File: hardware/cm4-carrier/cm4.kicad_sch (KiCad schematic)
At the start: 2 parts, among them J3 Raspberry Pi CM4

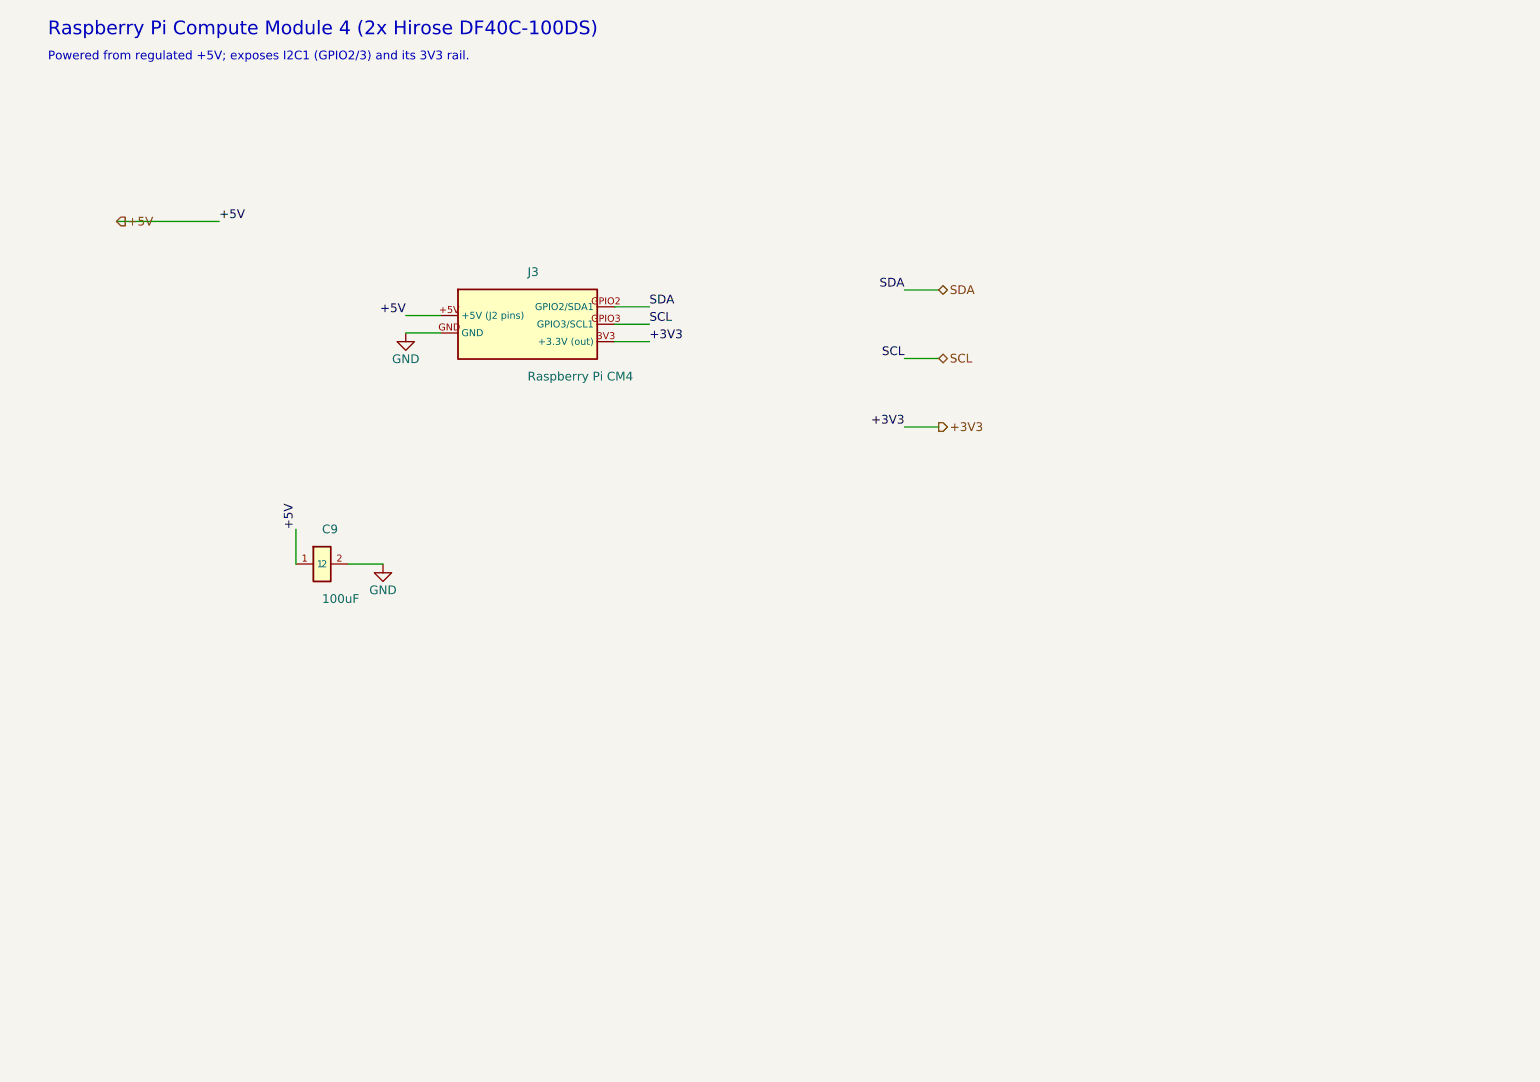
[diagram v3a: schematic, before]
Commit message: Add proper Raspberry Pi CM4 symbol and footprint
Replace the 5-pin CM4 placeholder with a real representation: the module is
modeled as its two physical 100-pin Hirose DF40 connectors (J3 = connector 1,
J4 = connector 2), each mapped to the carrier-side mating footprint
Connector_Hirose_DF40:Hirose_DF40C-100DP-0.4V_2x50-1MP_P0.4mm, with the full,
correctly-numbered CM4 pinout on every pin.

The board wires what it uses: all six +5V input pins, every GND on both
connectors, GPIO2/GPIO3 (I2C1) to the fuel gauge, and GPIO_VREF +
CM4_3.3V_Out for the 3.3 V I/O rail (which also feeds the I2C pull-ups). The
high-speed interfaces (PCIe, USB, Ethernet, HDMI, CSI/DSI) are left available
on the connectors. Adds C12 for CM4 5 V decoupling.

Pin maps were taken from the Kedarius RPi-CM4-Kicad symbol and cross-checked
against known CM4 facts (5 V on J1 77/79/81/83/85/87; GPIO2=pin58=SDA1;
GPIO3=pin56=SCL1; CM4_3.3V_Out on J1 84/86). Footprint verified against the
KiCad Connector_Hirose_DF40 library. README/BOM updated with CM4 bring-up
notes. No schematic-format change (KiCad 10, 20260306).

Co-Authored-By: Claude Opus 4.8 <noreply@anthropic.com>
Claude-Session: https://claude.ai/code/session_015B7X7FE461jFSRaiTFdnFt
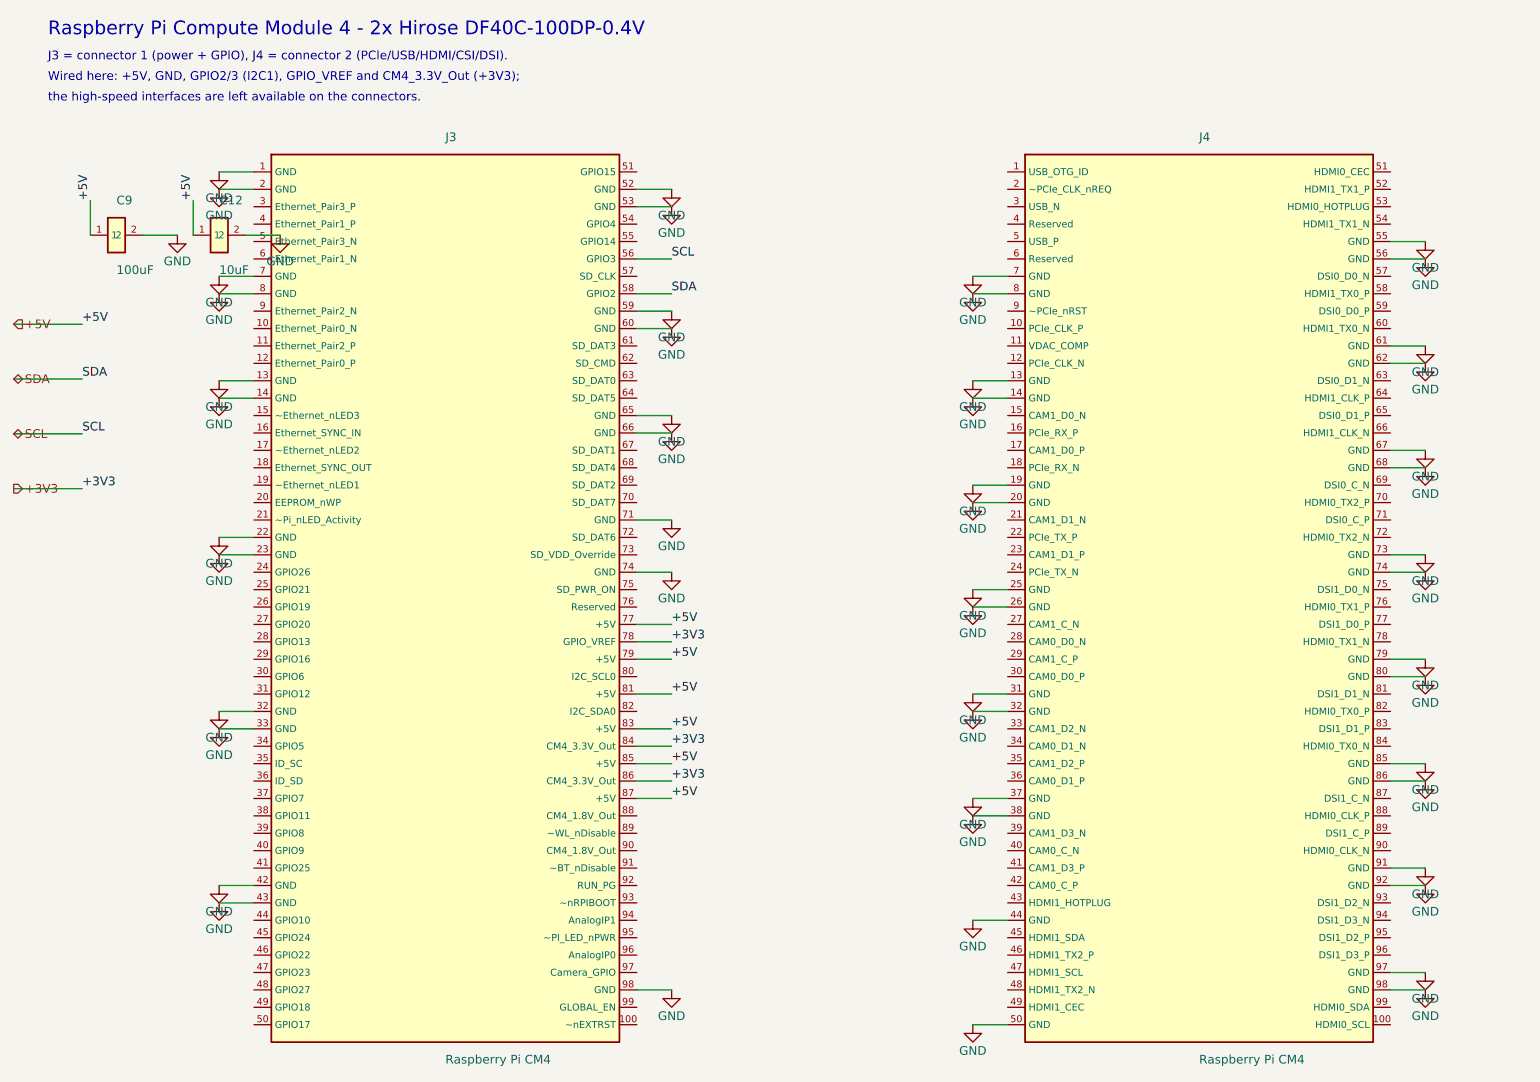
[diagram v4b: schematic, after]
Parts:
- removed J3: Raspberry Pi CM4, Connector_Hirose:Raspberry_Pi_CM4_DF40C-100DS, symbol carrier:Raspberry_Pi_CM4
- added C12: 10uF, Capacitor_SMD:C_0805_2012Metric, symbol carrier:C
- added J3: Raspberry Pi CM4, Connector_Hirose_DF40:Hirose_DF40C-100DP-0.4V_2x50-1MP_P0.4mm, symbol carrier:Raspberry_Pi_CM4_J1
- added J4: Raspberry Pi CM4, Connector_Hirose_DF40:Hirose_DF40C-100DP-0.4V_2x50-1MP_P0.4mm, symbol carrier:Raspberry_Pi_CM4_J2
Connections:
- net +3V3: now also J3.78 (GPIO_VREF), J3.84 (CM4_3.3V_Out), J3.86 (CM4_3.3V_Out)
- net +5V: now also C12.1, J3.77 (+5V), J3.79 (+5V), J3.81 (+5V), J3.83 (+5V), J3.85 (+5V), J3.87 (+5V)
- net GND: now also C12.2, J3.1 (GND), J3.13 (GND), J3.14 (GND), J3.2 (GND), J3.22 (GND), J3.23 (GND), J3.32 (GND), J3.33 (GND), J3.42 (GND), J3.43 (GND), J3.52 (GND), J3.53 (GND), J3.59 (GND), J3.60 (GND), J3.65 (GND), J3.66 (GND), J3.7 (GND), J3.71 (GND), J3.74 (GND), J3.8 (GND), J3.98 (GND), J4.13 (GND), J4.14 (GND), J4.19 (GND), J4.20 (GND), J4.25 (GND), J4.26 (GND), J4.31 (GND), J4.32 (GND), J4.37 (GND), J4.38 (GND), J4.44 (GND), J4.50 (GND), J4.55 (GND), J4.56 (GND), J4.61 (GND), J4.62 (GND), J4.67 (GND), J4.68 (GND), J4.7 (GND), J4.73 (GND), J4.74 (GND), J4.79 (GND), J4.8 (GND), J4.80 (GND), J4.85 (GND), J4.86 (GND), J4.91 (GND), J4.92 (GND), J4.97 (GND), J4.98 (GND)
- net SCL: now also J3.56 (GPIO3)
- net SDA: now also J3.58 (GPIO2)
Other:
- note added: "J3 = connector 1 (power + GPIO), J4 = connector 2 (PCIe/USB/HDMI/CSI/DSI)."
- note added: "Raspberry Pi Compute Module 4 - 2x Hirose DF40C-100DP-0.4V"
- note added: "Wired here: +5V, GND, GPIO2/3 (I2C1), GPIO_VREF and CM4_3.3V_Out (+3V3);"
- note added: "the high-speed interfaces are left available on the connectors."
- note removed: "Powered from regulated +5V; exposes I2C1 (GPIO2/3) and its 3V3 rail."
- note removed: "Raspberry Pi Compute Module 4 (2x Hirose DF40C-100DS)"

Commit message: Add two CSI-2 cameras with I2C mux and camera 3.3V rail
Add a new cameras.kicad_sch sub-sheet providing two Raspberry Pi CSI-2 camera
interfaces:

- J5 (CSI Camera 0) on the CM4's CAM0 (2-lane) interface; J6 (CSI Camera 1)
  on CAM1 (4-lane, two lanes wired) — standard 15-pin 1.0mm Pi camera FFC
  connectors (Connector_FFC-FPC:JUSHUO_AFA07-S15FCA-00...).
- PCA9544A I2C mux (U5) on the camera control bus I2C0 so the two identical-
  address sensors each sit on their own downstream channel (cam0 = ch0,
  cam1 = ch1, mux at 0x70).
- AP2112K-3.3 LDO (U7) generating a dedicated camera 3.3V rail from +5V, so
  two cameras don't overload the CM4's limited CM4_3.3V_Out. Adds per-channel
  and upstream I2C pull-ups and decoupling (R15-R20, C13-C15).

The CM4 sheet now exports the CAM0/CAM1 MIPI lanes (from J4), I2C0
(I2C_SCL0/SDA0) and four spare GPIOs (GPIO4-7, for the camera IO0/IO1
LED/enable lines) as global nets; the cameras sheet consumes them. Camera
FFC pinout and PCA9544A/DF40/FFC footprints were taken from KiCad's
libraries and the standard 15-pin CSI pinout.

Root gains a (pinless) Cameras sheet box. README/BOM updated. No
schematic-format change (KiCad 10, 20260306).

Co-Authored-By: Claude Opus 4.8 <noreply@anthropic.com>
Claude-Session: https://claude.ai/code/session_015B7X7FE461jFSRaiTFdnFt
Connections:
- net CAM1_D0_N: now reaches J4.15 (CAM1_D0_N)
- net CAM1_D0_P: now reaches J4.17 (CAM1_D0_P)
- net CAM1_D1_N: now reaches J4.21 (CAM1_D1_N)
- net CAM1_D1_P: now reaches J4.23 (CAM1_D1_P)
- net CAM1_C_N: now reaches J4.27 (CAM1_C_N)
- net CAM0_D0_N: now reaches J4.28 (CAM0_D0_N)
- net CAM1_C_P: now reaches J4.29 (CAM1_C_P)
- net CAM0_D0_P: now reaches J4.30 (CAM0_D0_P)
- net CAM0_D1_N: now reaches J4.34 (CAM0_D1_N)
- net CAM0_D1_P: now reaches J4.36 (CAM0_D1_P)
- net CAM0_C_N: now reaches J4.40 (CAM0_C_N)
- net CAM0_C_P: now reaches J4.42 (CAM0_C_P)
- net CAM1_IO0: now reaches J3.30 (GPIO6)
- net CAM0_IO1: now reaches J3.34 (GPIO5)
- net CAM1_IO1: now reaches J3.37 (GPIO7)
- net CAM0_IO0: now reaches J3.54 (GPIO4)
- net I2C0_SCL: now reaches J3.80 (I2C_SCL0)
- net I2C0_SDA: now reaches J3.82 (I2C_SDA0)

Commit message: Add a DSI display on the CM4's DSI0 interface
Add a Raspberry Pi DSI display connector (J7) to the peripherals sheet
(now "Cameras & Display"):

- J7 is a standard 15-pin 1.0mm RPi FFC driven by the CM4's DSI0 (2-lane)
  interface; the six DSI0 differential lanes are exported from the CM4 sheet
  (J4) as global nets alongside the camera lanes.
- The display's touch/controller I2C shares I2C0 on PCA9544A mux channel 2
  (SD2/SC2, previously unused), with its own pull-ups (R21/R22).
- IO0/IO1 (reset / backlight-enable) route to CM4 GPIO8/GPIO9; 3.3V logic
  comes from the existing camera LDO rail. The 5V panel/backlight power is
  supplied separately, as on the standard RPi 7-inch panel.

The mux is now 3 of 4 channels used (cam0/cam1/display). Root box renamed to
"Cameras & Display". README/BOM updated. No format change (KiCad 10, 20260306).

Co-Authored-By: Claude Opus 4.8 <noreply@anthropic.com>
Claude-Session: https://claude.ai/code/session_015B7X7FE461jFSRaiTFdnFt
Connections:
- net DSI0_D0_N: now reaches J4.57 (DSI0_D0_N)
- net DSI0_D0_P: now reaches J4.59 (DSI0_D0_P)
- net DSI0_D1_N: now reaches J4.63 (DSI0_D1_N)
- net DSI0_D1_P: now reaches J4.65 (DSI0_D1_P)
- net DSI0_C_N: now reaches J4.69 (DSI0_C_N)
- net DSI0_C_P: now reaches J4.71 (DSI0_C_P)
- net DSI0_IO0: now reaches J3.39 (GPIO8)
- net DSI0_IO1: now reaches J3.40 (GPIO9)

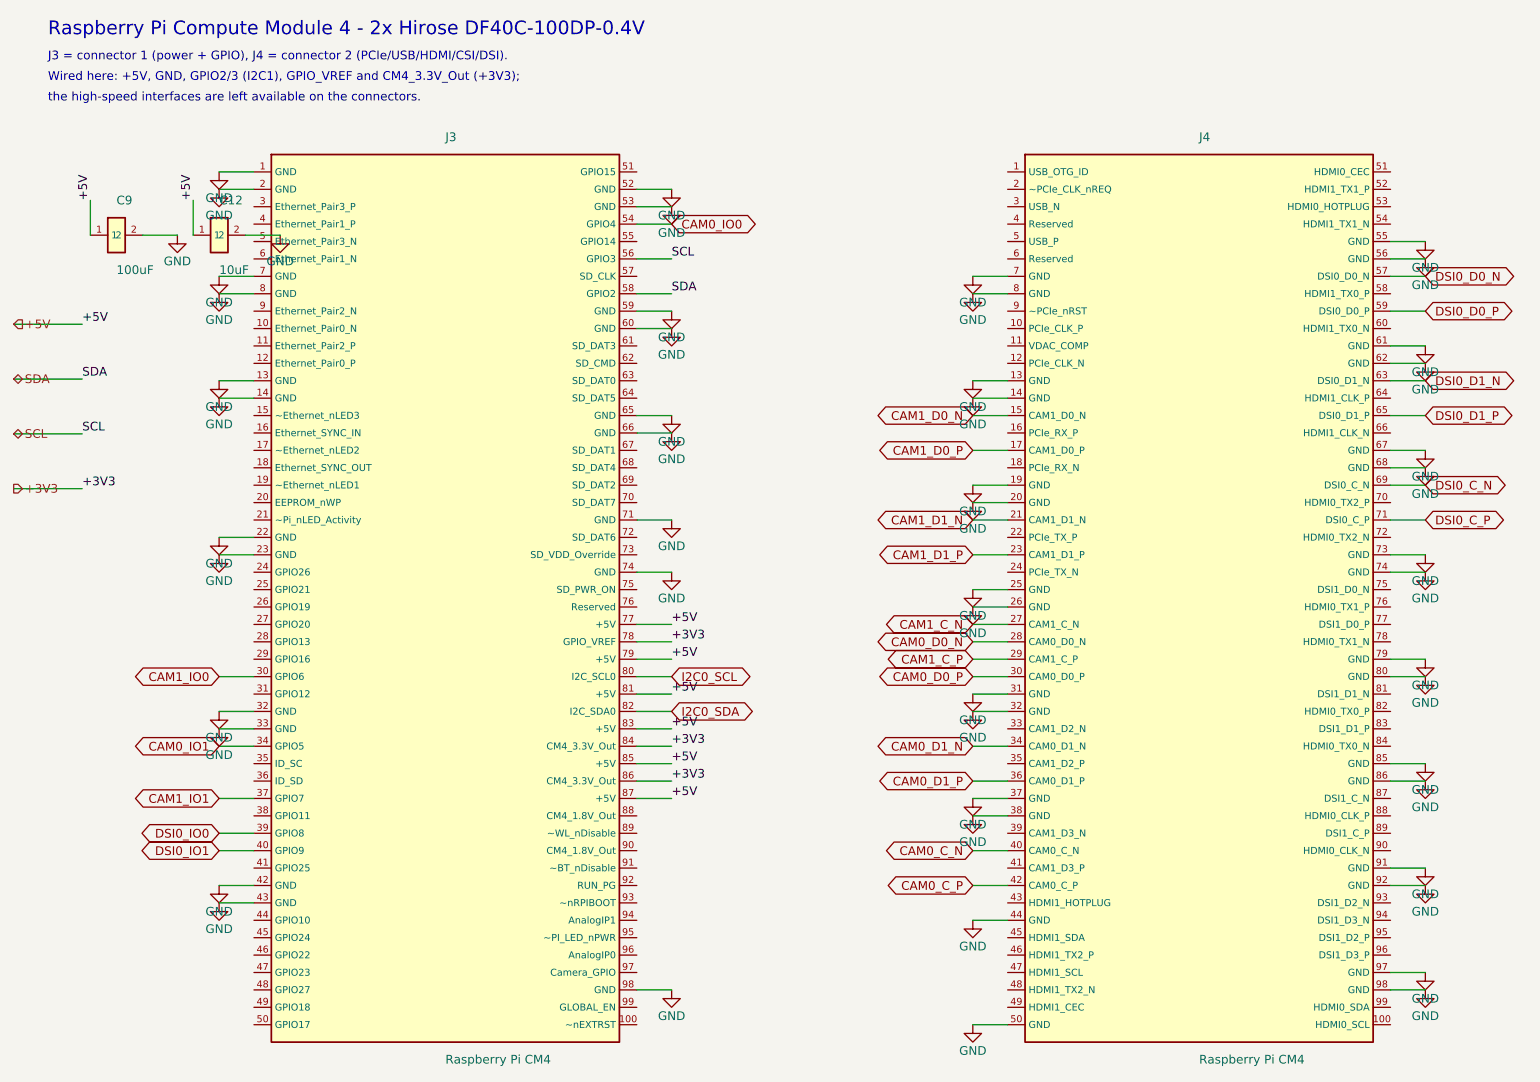
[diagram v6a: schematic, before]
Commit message: Add microSD boot (CM4 Lite) and CM4 bring-up controls
Add a boot_sd.kicad_sch sub-sheet with a microSD socket and the CM4 module
bring-up controls, so a CM4 Lite (no eMMC) can boot from card:

- microSD socket (J8, Hirose DM3D-SF) wired to the CM4 SD interface
  (SD_CLK/SD_CMD/SD_DAT0-3) with CMD/DAT pull-ups and a card-detect pull-up.
- SD 3.3V is gated by a high-side load switch (Q2 P-FET + Q3 N-FET) driven by
  the CM4's SD_PWR_ON (active high), with the card rail decoupled (C16/C17).
  SD_VDD_Override is defaulted low (3.3V card).
- Bring-up controls: GLOBAL_EN (power/enable, SW1), RUN_PG (run/reset, SW2)
  and nRPIBOOT (USB/rpiboot, SW3), each with a pull-up and momentary button;
  nEXTRST pulled up; power/activity LEDs (D3/D4) on PI_LED_nPWR / PI_LED_ACT.

The CM4 sheet now exports the SD interface and the GLOBAL_EN/RUN_PG/nRPIBOOT/
nEXTRST/PI_LED/SD_PWR_ON/SD_VDD_Override pins (from J1) as global nets; the
boot sheet consumes them. Pin directions were taken from the CM4 pin map;
microSD/SOT-23/tact-switch footprints from KiCad libraries.

Root gains a (pinless) Boot sheet box (page 8, now 7 sub-sheets). README/BOM
updated. No format change (KiCad 10, 20260306).

Co-Authored-By: Claude Opus 4.8 <noreply@anthropic.com>
Claude-Session: https://claude.ai/code/session_015B7X7FE461jFSRaiTFdnFt
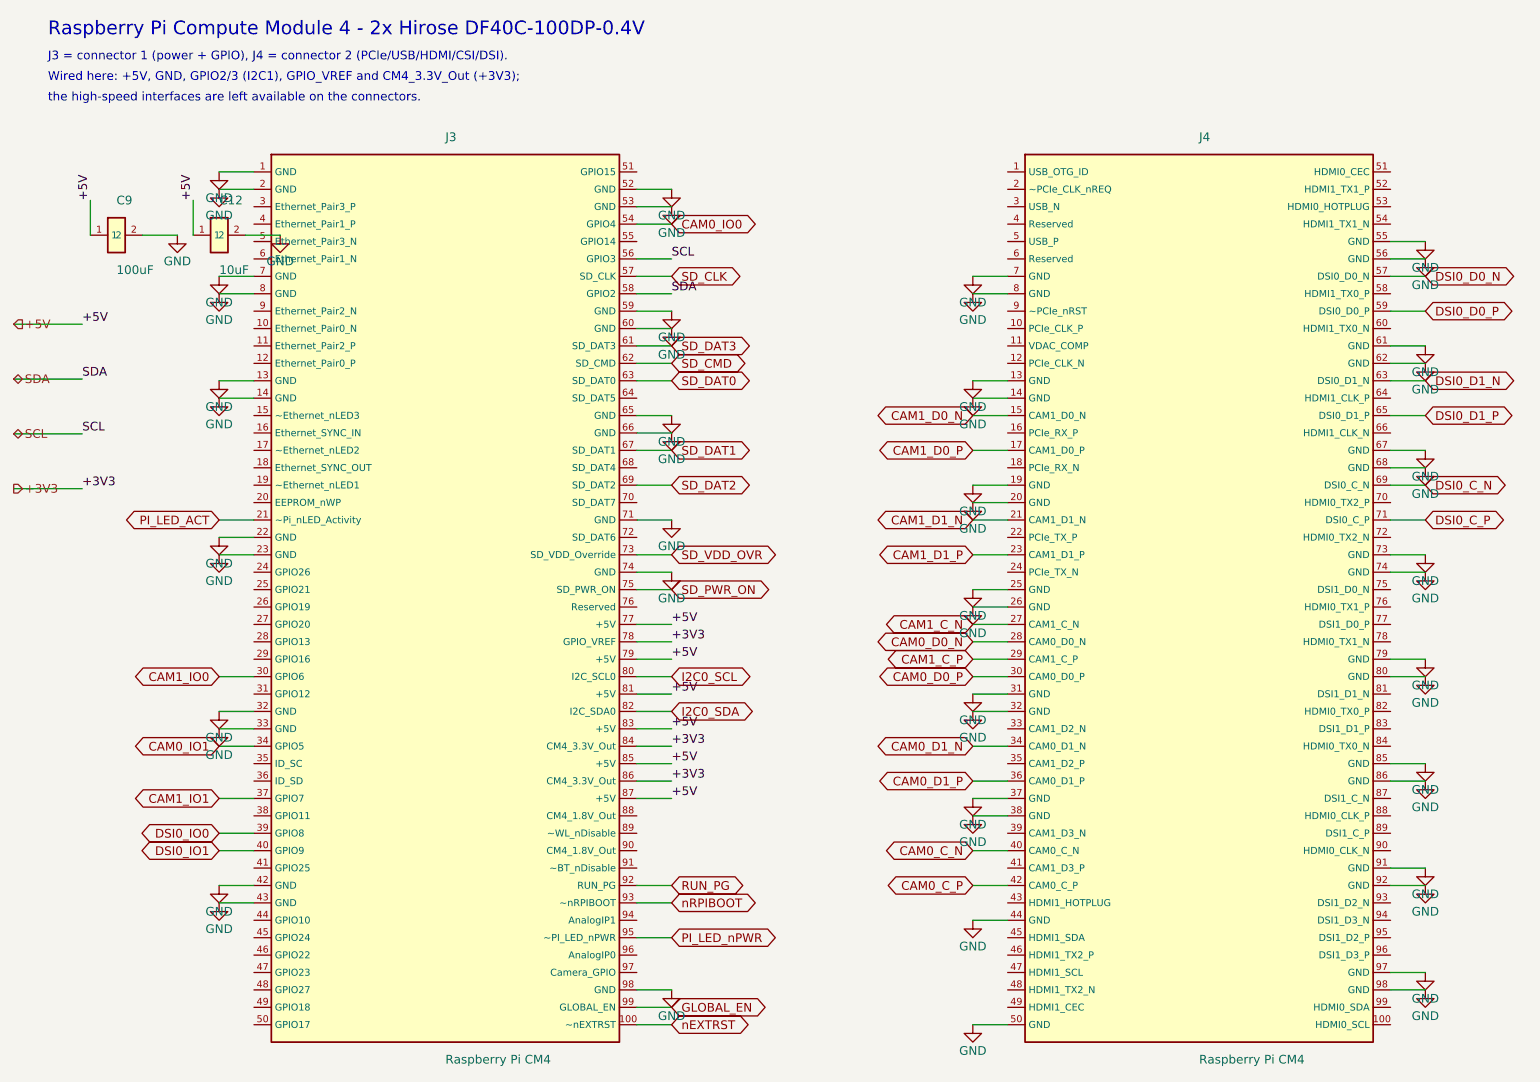
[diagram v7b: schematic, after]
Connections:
- net nEXTRST: now reaches J3.100 (~nEXTRST)
- net PI_LED_ACT: now reaches J3.21 (~Pi_nLED_Activity)
- net SD_CLK: now reaches J3.57 (SD_CLK)
- net SD_DAT3: now reaches J3.61 (SD_DAT3)
- net SD_CMD: now reaches J3.62 (SD_CMD)
- net SD_DAT0: now reaches J3.63 (SD_DAT0)
- net SD_DAT1: now reaches J3.67 (SD_DAT1)
- net SD_DAT2: now reaches J3.69 (SD_DAT2)
- net SD_VDD_OVR: now reaches J3.73 (SD_VDD_Override)
- net SD_PWR_ON: now reaches J3.75 (SD_PWR_ON)
- net RUN_PG: now reaches J3.92 (RUN_PG)
- net nRPIBOOT: now reaches J3.93 (~nRPIBOOT)
- net PI_LED_nPWR: now reaches J3.95 (~PI_LED_nPWR)
- net GLOBAL_EN: now reaches J3.99 (GLOBAL_EN)
